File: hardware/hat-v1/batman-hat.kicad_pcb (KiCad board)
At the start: 4 copper layers, 65 x 56.5 mm, 183 parts, among them J1 BATT pads, J2 Pi 40-pin (female, 11 mm stac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, J3 mPCIe 5.2H, J4 U.FL, J5 Tag-Connect TC2050, J6 PANEL BTN, Q1 CSD19537Q3, Q10 BSS138, Q2 BSS138, Q3 CSD17578Q3A, Q4 CSD17578Q3A, Q5 CSD17578Q3A, Q6 BSS138, Q7 BSS138, Q8 BSS138, Q9 BSS138, SW1 on-board PWR, U1 TPS26631RGER, U10 CAT24C32WI-GT3, U11 SLB9672XU2.0, U12 ATECC608C-TFLXTLS, U13 RV-3028-C7, U14 MAX-M10S-00B, U2 INA226AIDGSR, U3 LMR33640DDDAR, U4 LM74700QDBVRQ1, U5 LM74700QDBVRQ1, U6 LM74700QDBVRQ1, U7 TPS62933FDRLR, U8 INA226AIDGSR, U9 LTC2955ITS8-2#TRPBF

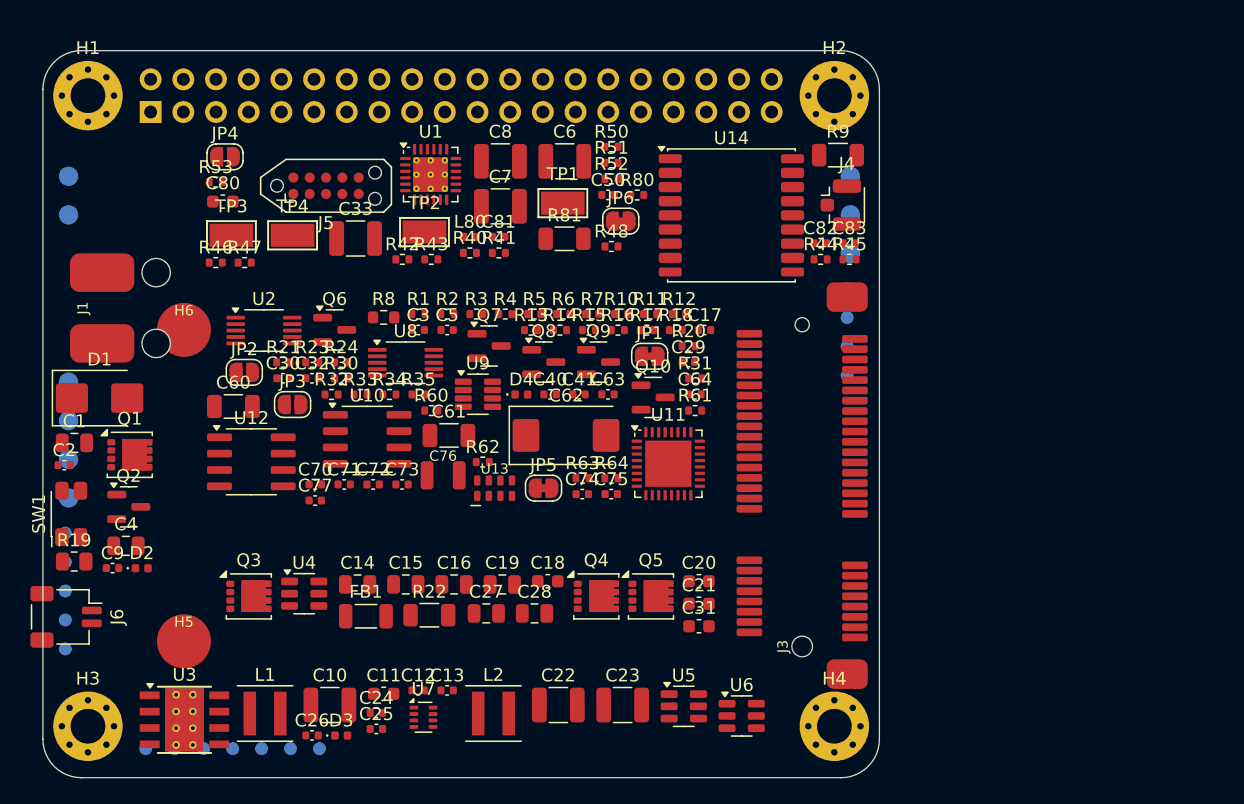
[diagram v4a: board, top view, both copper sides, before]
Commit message: HAT v1: GNSS 3-pin antenna supervisor (UBX-20053088 Fig 38) + RTC coin-cell backup
Antenna supply switched by LNA_EN, 10R sense, OPA333 comparator for open
detection, SCL/SDA reused for ANT_SHORT_N/ANT_DETECT. RTC backup moves to
a Seiko MS rechargeable cell with 1k series resistor (App Manual 7.3);
overlay trickle 15k. Cell footprint does not fit yet (floorplan).

Co-Authored-By: Claude Opus 5.5 <noreply@anthropic.com>
Claude-Session: https://claude.ai/code/session_01MLRuxTEmuMV82xcNLE62jW
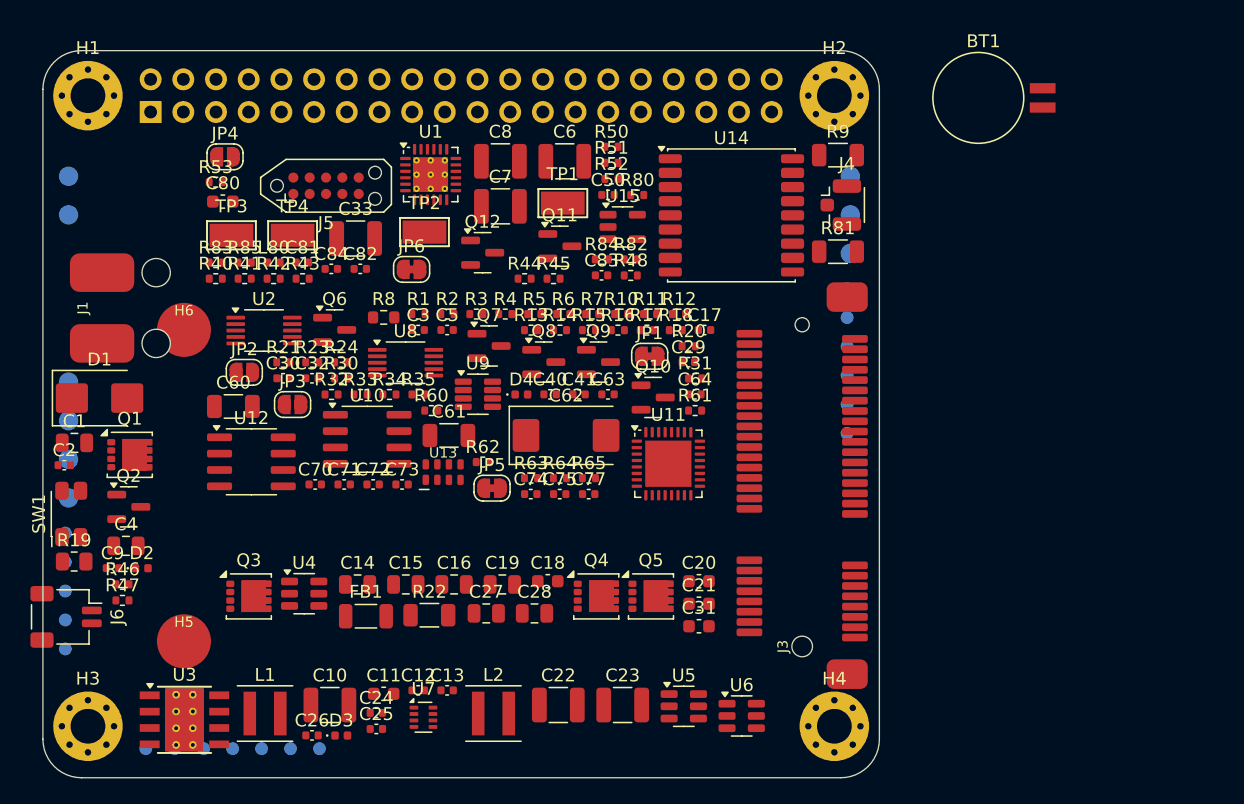
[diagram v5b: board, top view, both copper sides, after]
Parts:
- removed C76: CPH3225A 11mF, Seiko_CPH3225A
- added BT1: MS621FE 3V 5.5mAh, BatteryHolder_Seiko_MS621F, F.Cu at (177.7, 103.7)
- added C84: 100n 16V, C_0402_1005Metric, F.Cu at (122.4, 117.0)
- added Q11: Si2301CDS, SOT-23, F.Cu at (140.2, 115.2)
- added Q12: BSS138, SOT-23, F.Cu at (134.2, 115.7)
- added R65: 1k, R_0402_1005Metric, F.Cu at (142.4, 133.2)
- added R82: 560R, R_0402_1005Metric, F.Cu at (145.7, 116.2)
- added R83: 100k, R_0402_1005Metric, F.Cu at (113.4, 116.5)
- added R84: 100k, R_0402_1005Metric, F.Cu at (143.4, 116.2)
- added R85: 1k, R_0402_1005Metric, F.Cu at (115.7, 116.5)
- added TP30: K2+ (R22), TestPoint_Pad_D1.0mm, B.Cu at (119.2, 154.2)
- added TP31: K2- (R22), TestPoint_Pad_D1.0mm, B.Cu at (121.5, 154.2)
- added U15: OPA333AIDBVR, SOT-23-5, F.Cu at (145.0, 113.7)
- C82: value 10n 16V -> 10n 16V X7R
- R81: value 68R -> 10R
- TP16: value PWR_BTN_N -> GNSS_ANT_DET
- TP17: value LTC_KILL_N -> GNSS_ANT_SHORT_N
- TP18: value LTC_ENB -> PWR_BTN_N
- TP19: value EN_5V -> LTC_KILL_N
- TP20: value EN_3V3 -> LTC_ENB
- TP21: value PG_5V -> EN_5V
- TP22: value EF_FLT_N -> EN_3V3
- TP23: value EF_SHDN -> PG_5V
- TP24: value RTC_CLKOUT -> EF_FLT_N
- TP25: value RTC_INT_N -> EF_SHDN
- TP26: value K1+ (R9) -> RTC_CLKOUT
- TP27: value K1- (R9) -> RTC_INT_N
- TP28: value K2+ (R22) -> K1+ (R9)
- TP29: value K2- (R22) -> K1- (R9)
- moved TP16 62.5 mm to (162.5, 123.0)
- moved TP17 62.5 mm to (162.5, 125.2)
- moved TP24 60.9 mm to (110.2, 154.2)
- moved TP25 57.8 mm to (112.5, 154.2)
- moved TP26 54.7 mm to (162.5, 127.5)
- moved TP27 51.7 mm to (162.5, 129.7)
- moved C82 35.8 mm to (124.7, 117.0)
- moved R47 27.9 mm to (106.2, 142.7)
- moved R46 26.0 mm to (106.2, 141.5)
- moved R44 23.0 mm to (137.4, 117.7)
- moved R45 23.0 mm to (139.7, 117.7)
- moved R81 21.3 mm to (161.8, 115.6)
- moved C77 21.3 mm to (142.4, 134.5)
- moved R40 19.9 mm to (113.4, 117.7)
- moved R41 19.9 mm to (115.7, 117.7)
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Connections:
- net GNSS_BIAS renamed GNSS_ANT_FEED
- R81 pad 1: GNSS_VCCRF -> GNSS_ANT_SUP
- TP16 pad 1: PWR_BTN_N -> GNSS_ANT_DET
- TP17 pad 1: LTC_KILL_N -> GNSS_ANT_SHORT_N
- TP18 pad 1: LTC_ENB -> PWR_BTN_N
- TP19 pad 1: EN_5V -> LTC_KILL_N
- TP20 pad 1: EN_3V3 -> LTC_ENB
- TP21 pad 1: PG_5V -> EN_5V
- TP22 pad 1: EF_FLT_N -> EN_3V3
- TP23 pad 1: EF_SHDN -> PG_5V
- TP24 pad 1: RTC_CLKOUT -> EF_FLT_N
- TP25 pad 1: RTC_INT_N -> EF_SHDN
- TP26 pad 1: EF_OUT -> RTC_CLKOUT
- TP27 pad 1: VSYS -> RTC_INT_N
- TP28 pad 1: 3V3_BUCK -> EF_OUT
- TP29 pad 1: 3V3_SH -> VSYS
- U14 pad 13: (no net) -> GNSS_LNA_EN
- U14 pad 14: GNSS_VCCRF -> (no net)
- U14 pad 16: (no net) -> GNSS_ANT_DET
- U14 pad 17: (no net) -> GNSS_ANT_SHORT_N
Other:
- board text added: "DID NOT FIT (1)"

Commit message: HAT v1: keep the CPH3225A supercap for RTC backup (user decision)
Co-Authored-By: Claude Opus 5.5 <noreply@anthropic.com>
Claude-Session: https://claude.ai/code/session_01MLRuxTEmuMV82xcNLE62jW
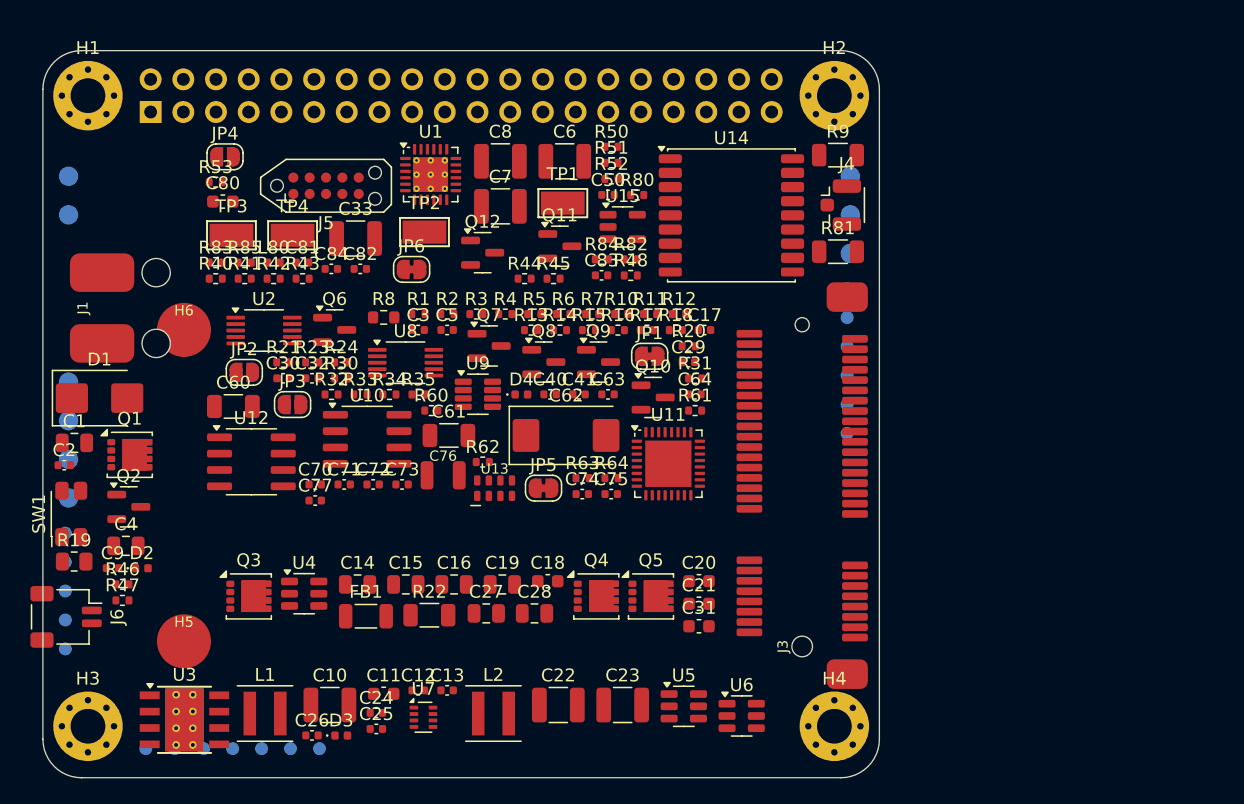
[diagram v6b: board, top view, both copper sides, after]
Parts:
- removed BT1: MS621FE 3V 5.5mAh, BatteryHolder_Seiko_MS621F
- removed R65: 1k, R_0402_1005Metric
- added C76: CPH3225A 11mF, Seiko_CPH3225A, F.Cu at (131.1, 133.0)
- moved C77 21.3 mm to (121.2, 135.0)
- moved U13 4.19 mm to (135.1, 134.0)
- moved C74 4.00 mm to (141.9, 134.5)
- moved C75 4.00 mm to (144.2, 134.5)
- moved JP5 4.00 mm to (138.9, 134.0)
- moved R63 4.00 mm to (141.9, 133.2)
- moved R64 4.00 mm to (144.2, 133.2)
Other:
- board text removed: "DID NOT FIT (1)"

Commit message: HAT v1: placed board (pre-routing) with In1 GND plane; ignore routing scratch files
Co-Authored-By: Claude Opus 5.5 <noreply@anthropic.com>
Claude-Session: https://claude.ai/code/session_01MLRuxTEmuMV82xcNLE62jW
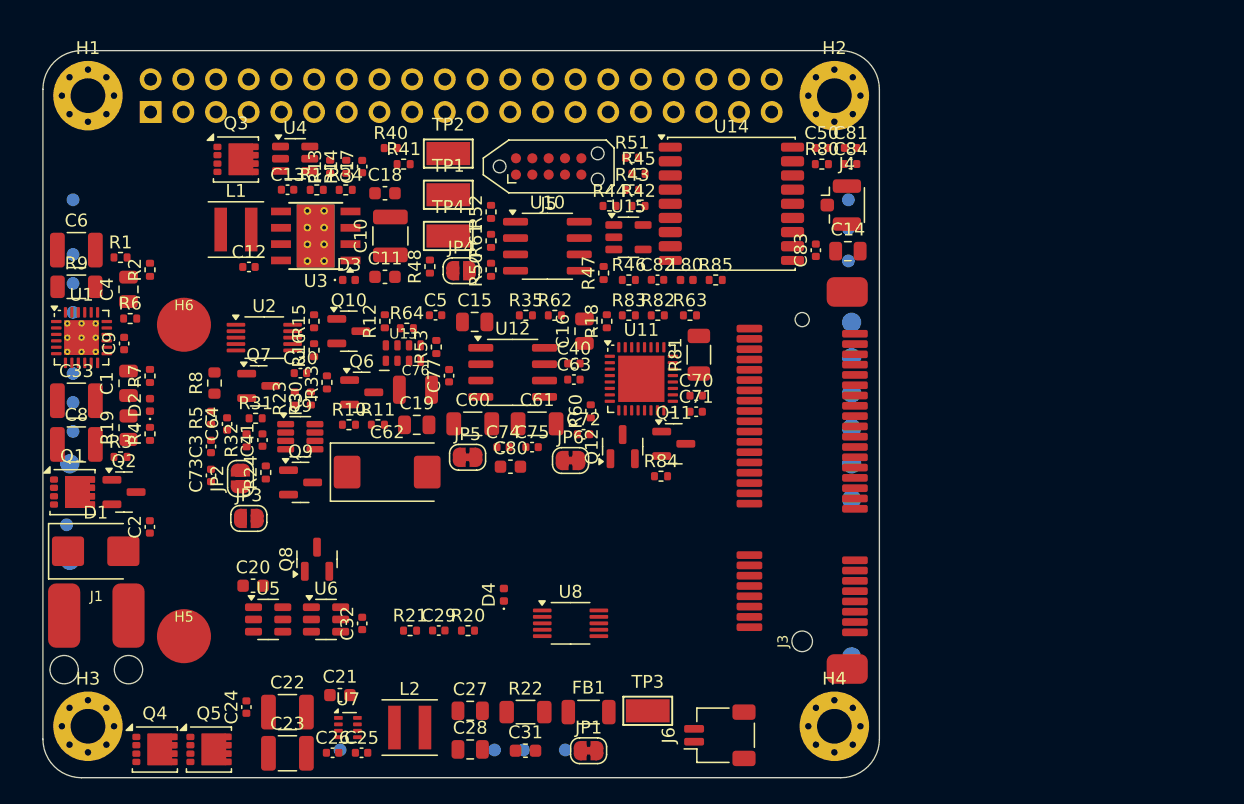
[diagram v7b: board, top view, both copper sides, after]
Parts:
- removed C7: 10u 50V X7R, C_1210_3225Metric
- removed SW1: on-board PWR, SW_SPST_EVQP7A
- moved TP8 63.6 mm to (162.8, 147.1)
- moved TP12 62.8 mm to (102.1, 132.1)
- moved TP5 61.9 mm to (162.8, 121.1)
- moved TP6 61.9 mm to (162.8, 123.9)
- moved TP26 61.3 mm to (102.3, 115.8)
- moved TP9 61.1 mm to (162.8, 126.6)
- moved TP13 60.9 mm to (162.8, 134.9)
- moved TP27 60.3 mm to (102.3, 134.6)
- moved R9 60.1 mm to (102.6, 118.3)
- moved J6 51.6 mm to (152.6, 153.2), turned to 90 degrees
- moved TP3 49.1 mm to (147.0, 151.3)
- moved C14 46.1 mm to (162.5, 115.6)
- moved R46 45.9 mm to (145.5, 117.8)
- moved R47 45.2 mm to (143.6, 117.3), turned to 90 degrees
- moved C81 43.5 mm to (162.8, 107.6)
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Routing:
- added copper zone on In1.Cu, net GND
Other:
- board text removed: "Pi 4 Wi-Fi keep-out (verify)"
- board text removed: "Wio-WM6108 card above (full-mini 30 x 51, underside ~3.1 mm)"
- board text removed: "bottom"
- board text removed: "left"
- board text removed: "top"
- board text removed: "under (<=1.9 mm tall)"
- board text removed: "under_edge (<=1.9 mm tall)"

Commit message: HAT v1: option D power tree - HaLow 3.3 V buck fed from the Pi 5 V rail
- TPS62933F input moved from the OR node to 5V_PI (HAT 5 V buck or Pi USB-C),
  as on the WM1302 HAT: the HaLow card still runs on USB-C only
- EN pulled up to the Pi 3.3 V through 100k: no back-feed into an unpowered Pi,
  HAT+ STANDBY turns the card off; LTC2955 off already removes 5 V
- removed: LM74700 x2 + FET x2 + VCAP x2 (OR-ing), BENCH jumper + Q9/R24, Q8,
  HAT ID EEPROM + WP jumper + pull-ups + decoupling, OR_NODE test point
- kept the battery-present divider (spec review #22)
- checker: HaLow EN set points; spec 5.5.5 power tree review; re-placed board

Co-Authored-By: Claude Opus 5.5 <noreply@anthropic.com>
Claude-Session: https://claude.ai/code/session_01MLRuxTEmuMV82xcNLE62jW
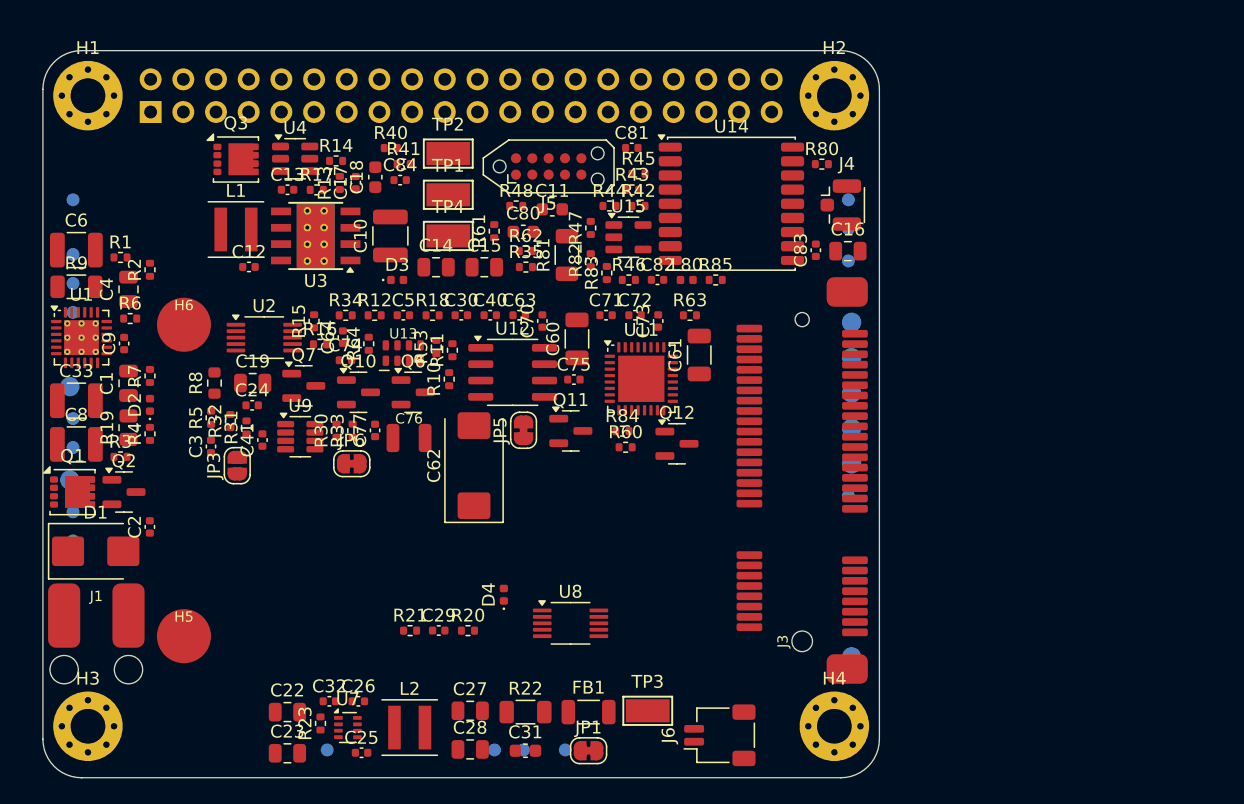
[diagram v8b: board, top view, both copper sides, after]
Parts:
- removed C20, C21: 220n 25V X7R, C_0603_1608Metric
- removed C50: 100n 16V, C_0402_1005Metric
- removed JP2: BENCH (open), SolderJumper-2_P1.3mm_Open_RoundedPad1.0x1.5mm
- removed JP4: EEP-WRITE (open), SolderJumper-2_P1.3mm_Open_RoundedPad1.0x1.5mm
- removed Q4, Q5: CSD17578Q3A, VSON-8_3.3x3.3mm_P0.65mm_NexFET
- removed Q8, Q9: BSS138, SOT-23
- removed R24: 100k, R_0402_1005Metric
- removed R50: 10k, R_0402_1005Metric
- removed R51, R52: 3.9k, R_0402_1005Metric
- removed TP31: K2- (R22), TestPoint_Pad_D1.0mm
- removed U10: CAT24C32WI-GT3, SOIC-8_3.9x4.9mm_P1.27mm
- removed U5, U6: LM74700QDBVRQ1, SOT-23-6
- C22, C23: value 10u 50V X7R -> 22u 10V X5R; footprint C_1210_3225Metric -> C_0805_2012Metric
- C24: value 100n 50V X7R -> 100n 16V
- R23: value 4.7M -> 100k
- TP10: value 3V3_SEC 3.2-3.4 -> 3V3_GNSS 3.2-3.4
- TP11: value 3V3_GNSS 3.2-3.4 -> VRTC 0-3.3
- TP12: value VRTC 0-3.3 -> GND
- TP13: value GND -> GNSS_RST_N; footprint TestPoint_Pad_D1.5mm -> TestPoint_Pad_D1.0mm
- TP14: value GNSS_RST_N -> GNSS_SAFEBOOT_N
- TP15: value GNSS_SAFEBOOT_N -> GNSS_ANT_DET
- TP16: value GNSS_ANT_DET -> GNSS_ANT_SHORT_N
- TP17: value GNSS_ANT_SHORT_N -> PWR_BTN_N
- TP18: value PWR_BTN_N -> LTC_KILL_N
- TP19: value LTC_KILL_N -> LTC_ENB
- TP20: value LTC_ENB -> EN_5V
- TP21: value EN_5V -> EN_3V3
- TP22: value EN_3V3 -> PG_5V
- TP23: value PG_5V -> EF_FLT_N
- TP24: value EF_FLT_N -> EF_SHDN
- TP25: value EF_SHDN -> RTC_CLKOUT
- TP26: value RTC_CLKOUT -> RTC_INT_N
- TP27: value RTC_INT_N -> K1+ (R9)
- TP28: value K1+ (R9) -> K1- (R9)
- TP29: value K1- (R9) -> K2+ (R22)
- TP30: value K2+ (R22) -> K2- (R22)
- TP7: value OR 5-17V -> 3V3_BUCK 3.25-3.40
- TP8: value 3V3_BUCK 3.25-3.40 -> 3V3_PI 3.2-3.4
- TP9: value 3V3_PI 3.2-3.4 -> 3V3_SEC 3.2-3.4
- moved TP28 61.9 mm to (162.6, 134.6)
- moved TP7 61.2 mm to (162.8, 147.1)
- moved TP6 60.8 mm to (102.1, 126.1)
- moved TP11 60.8 mm to (102.1, 133.4)
- moved TP12 60.8 mm to (162.8, 132.1)
- moved TP17 49.0 mm to (135.1, 154.3)
- moved TP22 47.5 mm to (102.3, 111.6)
- moved TP18 40.3 mm to (102.3, 130.8)
- moved TP29 39.6 mm to (137.3, 154.3)
- moved TP21 37.4 mm to (122.1, 154.3)
- moved C73 36.8 mm to (147.8, 121.0)
- moved C84 35.0 mm to (127.8, 110.1)
- moved C14 32.0 mm to (130.5, 116.8)
- moved R23 25.3 mm to (121.6, 152.3)
- moved C24 23.5 mm to (116.3, 127.6), turned to 0 degrees
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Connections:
- C22 pad 1: OR_NODE -> 5V_PI
- C23 pad 1: OR_NODE -> 5V_PI
- C24 pad 1: OR_NODE -> 5V_PI
- J2 pad 27: ID_SD -> (no net)
- J2 pad 28: ID_SC -> (no net)
- R23 pad 1: LTC_ENB -> 3V3_PI
- R23 pad 2: G33 -> EN_3V3
- TP10 pad 1: 3V3_SEC -> 3V3_GNSS
- TP11 pad 1: 3V3_GNSS -> VRTC
- TP12 pad 1: VRTC -> GND
- TP13 pad 1: GND -> GNSS_RST_N
- TP14 pad 1: GNSS_RST_N -> GNSS_SAFEBOOT_N
- TP15 pad 1: GNSS_SAFEBOOT_N -> GNSS_ANT_DET
- TP16 pad 1: GNSS_ANT_DET -> GNSS_ANT_SHORT_N
- TP17 pad 1: GNSS_ANT_SHORT_N -> PWR_BTN_N
- TP18 pad 1: PWR_BTN_N -> LTC_KILL_N
- TP19 pad 1: LTC_KILL_N -> LTC_ENB
- TP20 pad 1: LTC_ENB -> EN_5V
- TP21 pad 1: EN_5V -> EN_3V3
- TP22 pad 1: EN_3V3 -> PG_5V
- TP23 pad 1: PG_5V -> EF_FLT_N
- TP24 pad 1: EF_FLT_N -> EF_SHDN
- TP25 pad 1: EF_SHDN -> RTC_CLKOUT
- TP26 pad 1: RTC_CLKOUT -> RTC_INT_N
- TP27 pad 1: RTC_INT_N -> EF_OUT
- TP28 pad 1: EF_OUT -> VSYS
- TP29 pad 1: VSYS -> 3V3_BUCK
- TP30 pad 1: 3V3_BUCK -> 3V3_SH
- TP7 pad 1: OR_NODE -> 3V3_BUCK
- TP8 pad 1: 3V3_BUCK -> 3V3_PI
- TP9 pad 1: 3V3_PI -> 3V3_SEC
- U7 pad 3: OR_NODE -> 5V_PI
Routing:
- removed copper zone on In1.Cu, net GND
